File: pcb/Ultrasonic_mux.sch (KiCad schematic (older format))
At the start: 70 parts, among them J0 DB9_Male, J1 DB9_Male, J10 Conn_01x03_Male, J11 Conn_01x03_Male, J12 Conn_01x03_Male, J13 Conn_01x03_Male, J14 Conn_01x03_Male, J15 Conn_01x03_Male, J2 DB9_Male, J3 DB9_Male, J4 DB9_Male, J5 DB9_Male, P1 , P12 , P27 , P28 , P3 , P5 , Q0 MMBT3904, Q1 MMBT3904, Q2 MMBT3904, Q3 MMBT3904, Q4 MMBT3904, Q5 MMBT3904, U1 FeatherM0

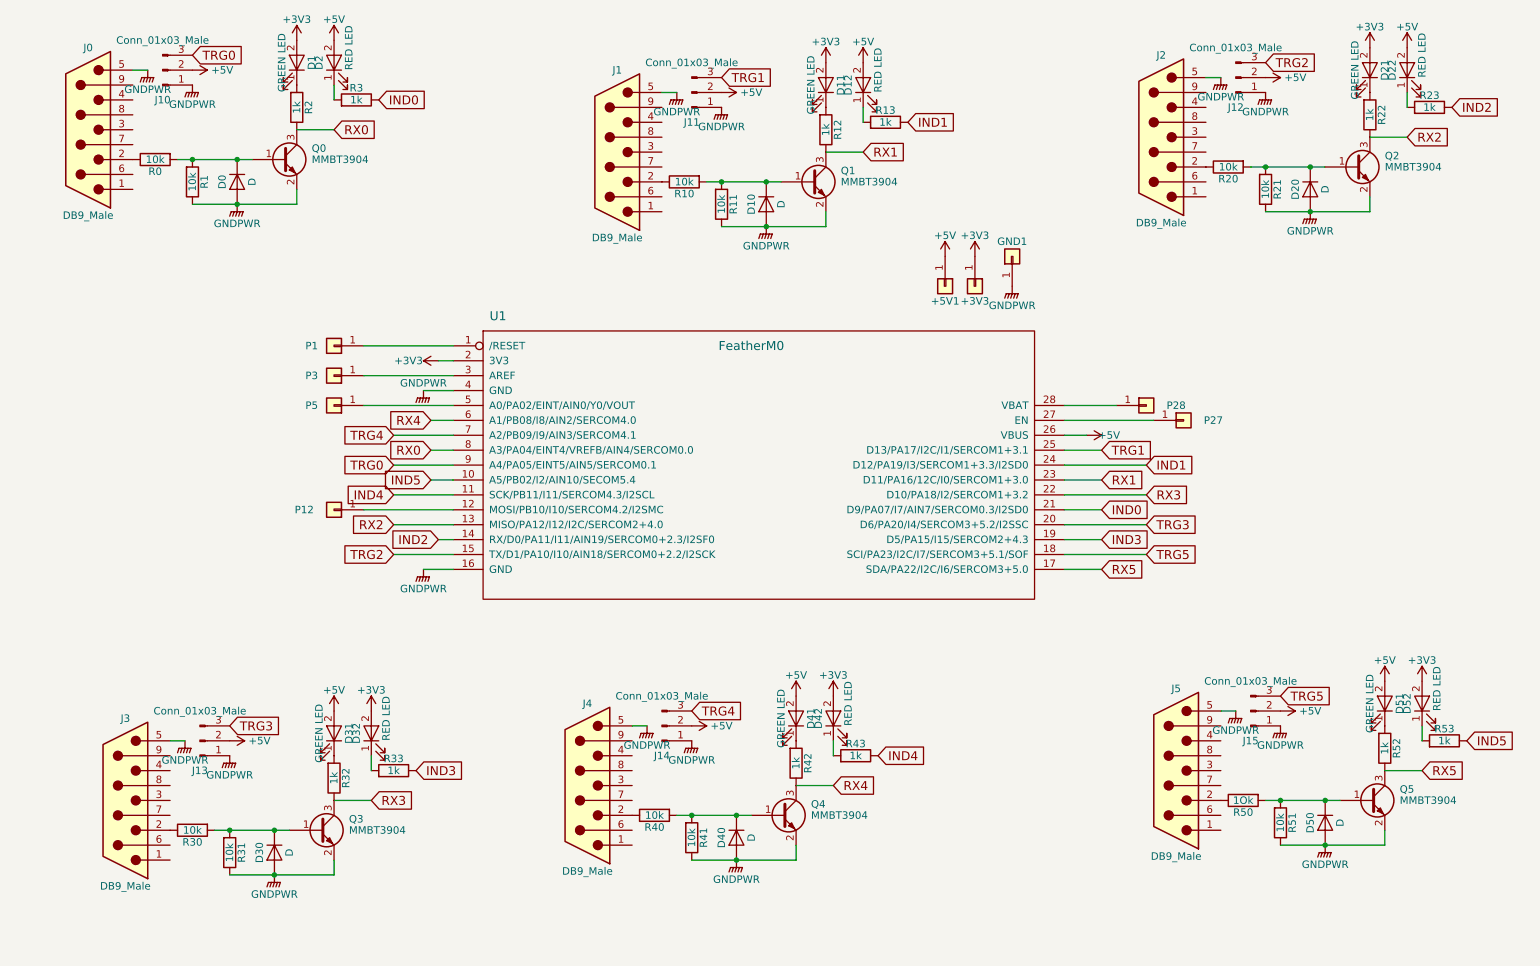
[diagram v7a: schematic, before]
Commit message: Finished footprints, starting layout of board.
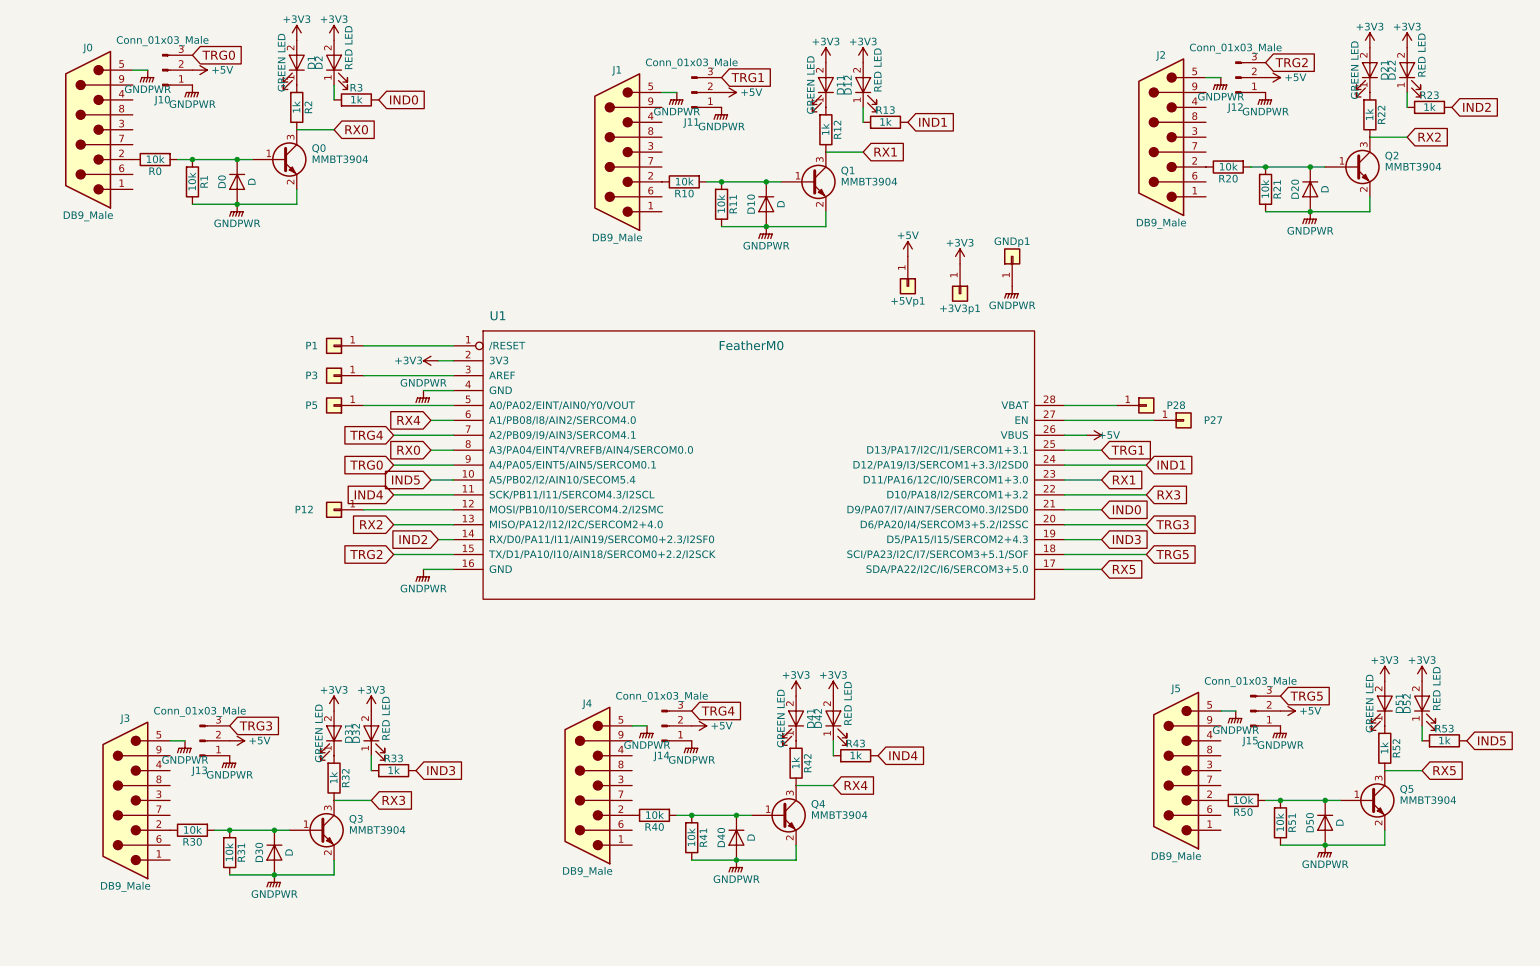
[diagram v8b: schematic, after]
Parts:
- +3V3p1: renamed from +3V3; footprint (none) -> Pin_Headers:Pin_Header_Angled_1x01_Pitch2.54mm
- +5Vp1: renamed from +5V1; footprint (none) -> Pin_Headers:Pin_Header_Angled_1x01_Pitch2.54mm
- D0, D10, D20, D30, D40, D50: footprint (none) -> Diodes_SMD:D_SOT-23_ANK
- GNDp1: renamed from GND1; footprint (none) -> Pin_Headers:Pin_Header_Angled_1x01_Pitch2.54mm
- J0, J1, J2, J3, J4, J5: footprint (none) -> Connectors_DSub:DSUB-9_Male_Vertical_Pitch2.77x2.84mm_MountingHoles
- J10, J11, J12, J13, J14, J15: footprint (none) -> Pin_Headers:Pin_Header_Straight_1x03_Pitch2.54mm
- P1, P12, P27, P28, P3, P5: footprint (none) -> Pin_Headers:Pin_Header_Straight_1x01_Pitch2.54mm
- R0, R1, R10, R11, R12, R13, R2, R20, R21, R22, R23, R3, R30, R31, R32, R33, R40, R41, R42, R43, R50, R51, R52, R53: footprint (none) -> Resistors_SMD:R_0805_HandSoldering
- U1: footprint (none) -> Feather M0:featherm0
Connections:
- net +3V3: now also D12.2 (A), D2.2 (A), D22.2 (A), D31.2 (A), D41.2 (A), D51.2 (A)
- net +5V: no longer D12.2 (A), D2.2 (A), D22.2 (A), D31.2 (A), D41.2 (A), D51.2 (A)
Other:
- moved on the sheet: +3V3p1, +5Vp1
